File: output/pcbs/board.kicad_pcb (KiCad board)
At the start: 2 copper layers, 134.2 x 121.1 mm, 59 parts

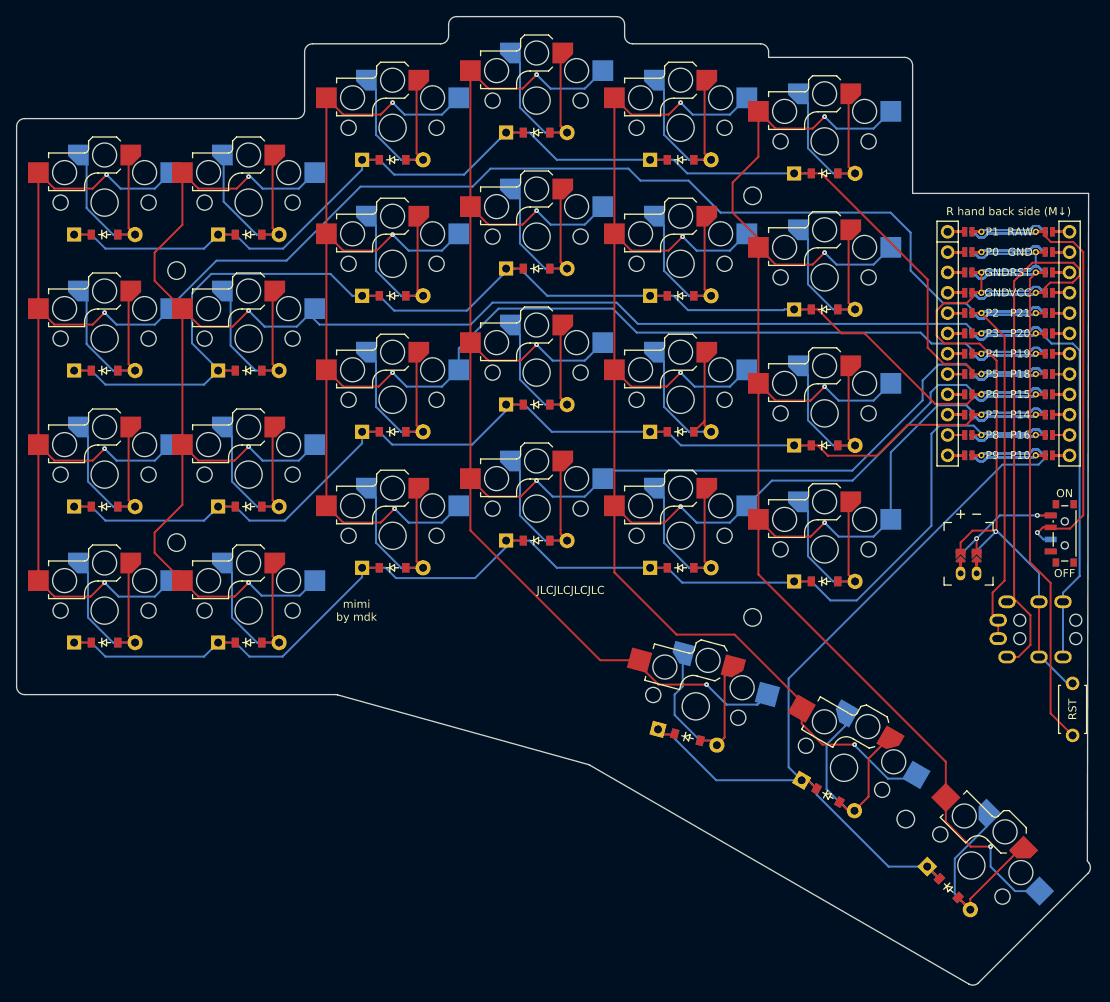
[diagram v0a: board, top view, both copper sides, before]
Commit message: trrs: enable back symmetric + serial pin
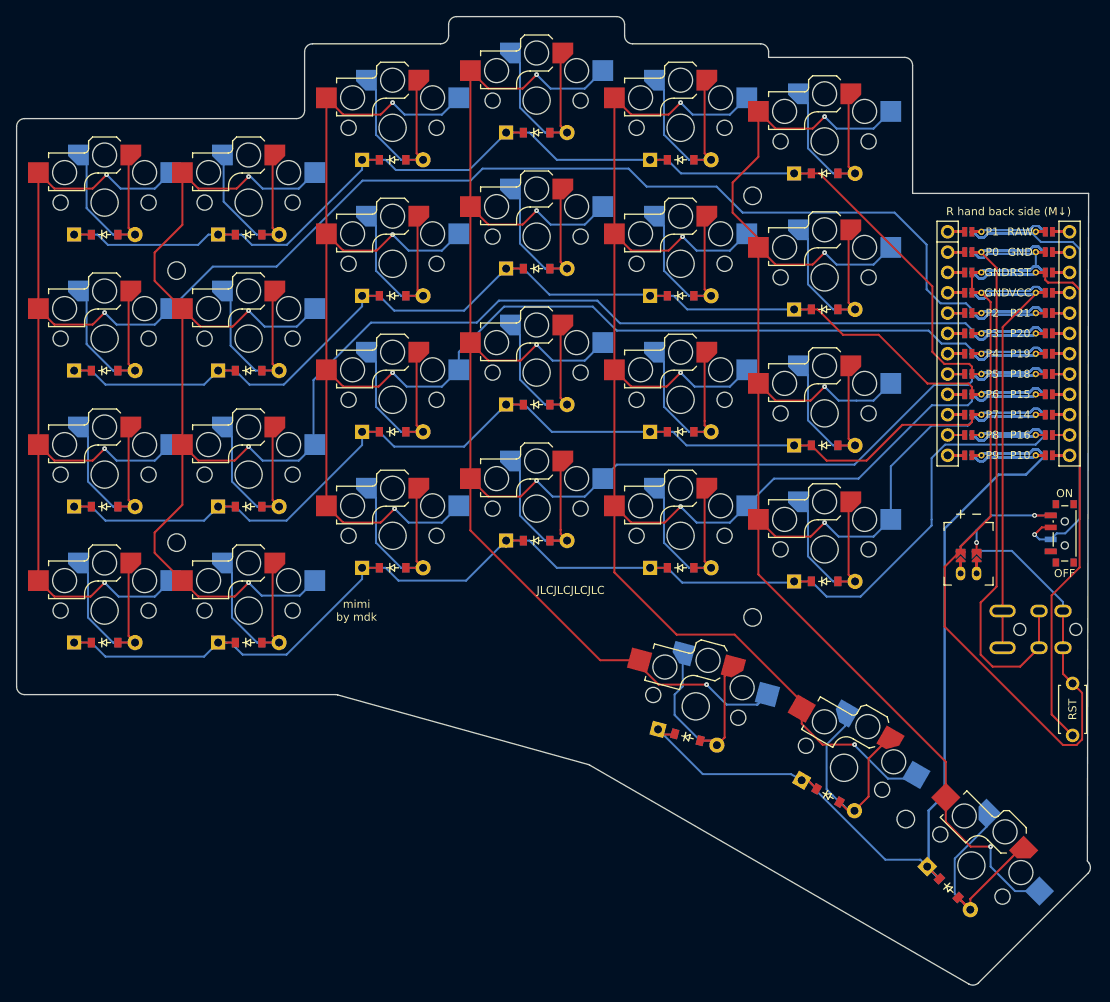
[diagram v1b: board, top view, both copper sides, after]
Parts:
- TRRS1: footprint ceoloide:trrs_pj320a (reversible) -> ceoloide:trrs_pj320a (reversible, symmetric)
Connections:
- TRRS1 pad 2: P3 -> GND
- TRRS1 pad 3: GND -> P0
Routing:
- net P0: track 67.8 -> 133.3 mm
- net P3: track 112.7 -> 67.8 mm
- net P2: track 111.2 -> 67.8 mm
- net GND: track 280.4 -> 307.9 mm, vias 1 -> 0
- net VCC: track 134.6 -> 113.9 mm
- net P6: track 225.8 -> 211.7 mm
- net P20: track 289.6 -> 299.7 mm
- net P9: track 176.8 -> 182.7 mm
- net P8: track 224.9 -> 229.9 mm
- net RST: track 128.1 -> 131.7 mm
- net BAT_P: track 16.3 -> 19.8 mm
- net P18: track 309.8 -> 306.6 mm
- net P14: track 288.8 -> 286.1 mm
- net RAW: track 115.6 -> 117.5 mm
- net P15: track 293.0 -> 291.5 mm
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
